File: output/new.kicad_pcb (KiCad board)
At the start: 2 copper layers, 96 parts

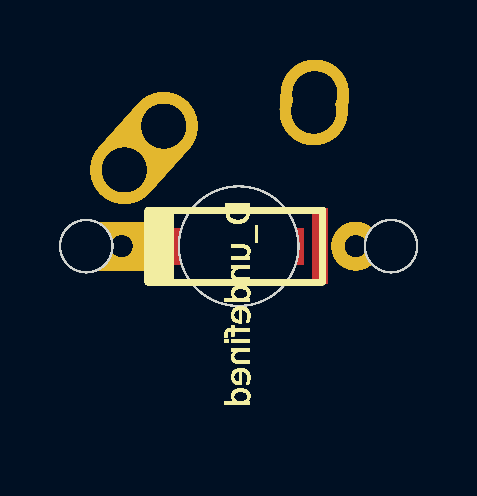
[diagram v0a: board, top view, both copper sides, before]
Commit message: feat: generate PCB component names
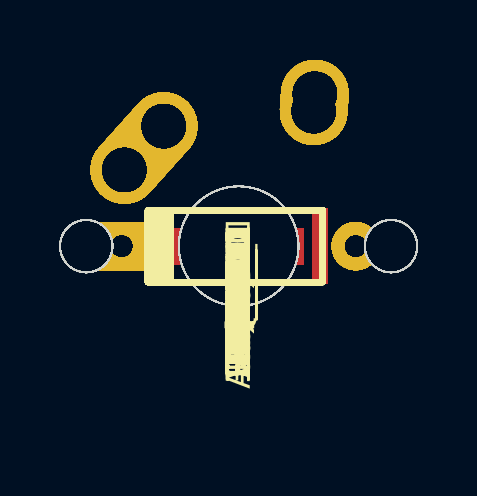
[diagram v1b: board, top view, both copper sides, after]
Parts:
- removed D_undefined (x48): D, keyboard_parts:D_SOD123_axial
- removed K_ (x48): KEYSW, MX_Alps_Hybrid:MX-[object
- added D_A, D_ALT, D_ALT1, D_B, D_BS, D_C, D_CAPS, D_COMMA, D_D, D_DOT, D_E, D_ENTER, D_ESC, D_F, D_FN, D_G, D_H, D_I, D_J, D_K, D_L, D_M, D_M2, D_M3, D_M4, D_N, D_O, D_OPT, D_OPT1, D_P, D_Q, D_QUOTE, D_R, D_S, D_SEMIC, D_SHIFT, D_SHIFT1, D_SLASH, D_SPACE, D_T, D_U, D_V, D_W, D_X, D_Y, D_Z, D_[, D_]: D, keyboard_parts:D_SOD123_axial, F.Cu at (nan, nan)
- added K_A, K_ALT, K_ALT1, K_B, K_BS, K_C, K_CAPS, K_COMMA, K_D, K_DOT, K_E, K_ENTER, K_ESC, K_F, K_FN, K_G, K_H, K_I, K_J, K_K, K_L, K_M, K_M2, K_M3, K_M4, K_N, K_O, K_OPT, K_OPT1, K_P, K_Q, K_QUOTE, K_R, K_S, K_SEMIC, K_SHIFT, K_SHIFT1, K_SLASH, K_SPACE, K_T, K_U, K_V, K_W, K_X, K_Y, K_Z, K_[, K_]: KEYSW, MX_Alps_Hybrid:MX-[object, F.Cu at (nan, nan)

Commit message: feat: PCB keyboard layout
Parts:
- removed D_[, D_]: D, keyboard_parts:D_SOD123_axial
- removed the K_A at (nan, nan)
- removed the K_ALT at (nan, nan)
- removed the K_B at (nan, nan)
- removed the K_BS at (nan, nan)
- removed the K_C at (nan, nan)
- removed the K_CAPS at (nan, nan)
- removed the K_COMMA at (nan, nan)
- removed the K_D at (nan, nan)
- removed the K_DOT at (nan, nan)
- removed the K_E at (nan, nan)
- removed the K_ENTER at (nan, nan)
- removed the K_ESC at (nan, nan)
- removed the K_F at (nan, nan)
- removed the K_FN at (nan, nan)
- removed the K_G at (nan, nan)
- removed the K_H at (nan, nan)
- removed the K_I at (nan, nan)
- removed the K_J at (nan, nan)
- removed the K_K at (nan, nan)
- removed the K_L at (nan, nan)
- removed the K_M at (nan, nan)
- removed the K_N at (nan, nan)
- removed the K_O at (nan, nan)
- removed the K_OPT at (nan, nan)
- removed the K_P at (nan, nan)
- removed the K_Q at (nan, nan)
- removed the K_QUOTE at (nan, nan)
- removed the K_R at (nan, nan)
- removed the K_S at (nan, nan)
- removed the K_SEMIC at (nan, nan)
- removed the K_SHIFT at (nan, nan)
- removed the K_SLASH at (nan, nan)
- removed the K_SPACE at (nan, nan)
- removed the K_T at (nan, nan)
- removed the K_U at (nan, nan)
- removed the K_V at (nan, nan)
- removed the K_W at (nan, nan)
- removed the K_X at (nan, nan)
- removed the K_Y at (nan, nan)
- removed the K_Z at (nan, nan)
- removed K_[, K_]: KEYSW, MX_Alps_Hybrid:MX-[object
- added D_CBRAC: D, keyboard_parts:D_SOD123_axial, F.Cu at (233.9, 10.0)
- added D_OBRAC: D, keyboard_parts:D_SOD123_axial, F.Cu at (252.9, 10.0)
- added K_A: KEYSW, MX_Alps_Hybrid:MX-1U-NoLED, F.Cu at (57.1, 28.6)
- added K_ALT: KEYSW, MX_Alps_Hybrid:MX-1.25U-NoLED, F.Cu at (83.3, 66.7)
- added K_B: KEYSW, MX_Alps_Hybrid:MX-1U-NoLED, F.Cu at (142.9, 47.6)
- added K_BS: KEYSW, MX_Alps_Hybrid:MX-1U-NoLED, F.Cu at (281.0, 9.53)
- added K_C: KEYSW, MX_Alps_Hybrid:MX-1U-NoLED, F.Cu at (104.8, 47.6)
- added K_CAPS: KEYSW, MX_Alps_Hybrid:MX-1.25U-NoLED, F.Cu at (35.7, 28.6)
- added K_CBRAC: KEYSW, MX_Alps_Hybrid:MX-1U-NoLED, F.Cu at (242.9, 9.53)
- added K_COMMA: KEYSW, MX_Alps_Hybrid:MX-1U-NoLED, F.Cu at (200.0, 47.6)
- added K_D: KEYSW, MX_Alps_Hybrid:MX-1U-NoLED, F.Cu at (95.2, 28.6)
- added K_DOT: KEYSW, MX_Alps_Hybrid:MX-1U-NoLED, F.Cu at (219.1, 47.6)
- added K_E: KEYSW, MX_Alps_Hybrid:MX-1U-NoLED, F.Cu at (90.5, 9.53)
- added K_ENTER: KEYSW, MX_Alps_Hybrid:MX-1.75U-NoLED, F.Cu at (273.8, 28.6)
- added K_ESC: KEYSW, MX_Alps_Hybrid:MX-1U-NoLED, F.Cu at (33.3, 9.53)
- added K_F: KEYSW, MX_Alps_Hybrid:MX-1U-NoLED, F.Cu at (114.3, 28.6)
- added K_FN: KEYSW, MX_Alps_Hybrid:MX-1U-NoLED, F.Cu at (281.0, 47.6)
- added K_G: KEYSW, MX_Alps_Hybrid:MX-1U-NoLED, F.Cu at (133.3, 28.6)
- added K_H: KEYSW, MX_Alps_Hybrid:MX-1U-NoLED, F.Cu at (152.4, 28.6)
- added K_I: KEYSW, MX_Alps_Hybrid:MX-1U-NoLED, F.Cu at (185.7, 9.53)
- added K_J: KEYSW, MX_Alps_Hybrid:MX-1U-NoLED, F.Cu at (171.4, 28.6)
- added K_K: KEYSW, MX_Alps_Hybrid:MX-1U-NoLED, F.Cu at (190.5, 28.6)
- added K_L: KEYSW, MX_Alps_Hybrid:MX-1U-NoLED, F.Cu at (209.6, 28.6)
- added K_M: KEYSW, MX_Alps_Hybrid:MX-1U-NoLED, F.Cu at (181.0, 47.6)
- added K_N: KEYSW, MX_Alps_Hybrid:MX-1U-NoLED, F.Cu at (161.9, 47.6)
- added K_O: KEYSW, MX_Alps_Hybrid:MX-1U-NoLED, F.Cu at (204.8, 9.53)
- added K_OBRAC: KEYSW, MX_Alps_Hybrid:MX-1U-NoLED, F.Cu at (261.9, 9.53)
- added K_OPT: KEYSW, MX_Alps_Hybrid:MX-1U-NoLED, F.Cu at (61.9, 66.7)
- added K_P: KEYSW, MX_Alps_Hybrid:MX-1U-NoLED, F.Cu at (223.8, 9.53)
- added K_Q: KEYSW, MX_Alps_Hybrid:MX-1U-NoLED, F.Cu at (52.4, 9.53)
- added K_QUOTE: KEYSW, MX_Alps_Hybrid:MX-1U-NoLED, F.Cu at (247.7, 28.6)
- added K_R: KEYSW, MX_Alps_Hybrid:MX-1U-NoLED, F.Cu at (109.5, 9.53)
- added K_S: KEYSW, MX_Alps_Hybrid:MX-1U-NoLED, F.Cu at (76.2, 28.6)
- added K_SEMIC: KEYSW, MX_Alps_Hybrid:MX-1U-NoLED, F.Cu at (228.6, 28.6)
- added K_SHIFT: KEYSW, MX_Alps_Hybrid:MX-1.75U-NoLED, F.Cu at (40.5, 47.6)
- added K_SLASH: KEYSW, MX_Alps_Hybrid:MX-1U-NoLED, F.Cu at (238.1, 47.6)
- added K_SPACE: KEYSW, MX_Alps_Hybrid:MX-6.25U-NoLED, F.Cu at (154.8, 66.7)
- added K_T: KEYSW, MX_Alps_Hybrid:MX-1U-NoLED, F.Cu at (128.6, 9.53)
- added K_U: KEYSW, MX_Alps_Hybrid:MX-1U-NoLED, F.Cu at (166.7, 9.53)
- added K_V: KEYSW, MX_Alps_Hybrid:MX-1U-NoLED, F.Cu at (123.8, 47.6)
- added K_W: KEYSW, MX_Alps_Hybrid:MX-1U-NoLED, F.Cu at (71.4, 9.53)
- added K_X: KEYSW, MX_Alps_Hybrid:MX-1U-NoLED, F.Cu at (85.7, 47.6)
- added K_Y: KEYSW, MX_Alps_Hybrid:MX-1U-NoLED, F.Cu at (147.6, 9.53)
- added K_Z: KEYSW, MX_Alps_Hybrid:MX-1U-NoLED, F.Cu at (66.7, 47.6)
- K_ALT1, K_SHIFT1: footprint MX_Alps_Hybrid:MX-[object -> MX_Alps_Hybrid:MX-1.25U-NoLED
- K_M2, K_M3, K_M4, K_OPT1: footprint MX_Alps_Hybrid:MX-[object -> MX_Alps_Hybrid:MX-1U-NoLED

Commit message: feat: added planes and frames to the PCB
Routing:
- added copper zone on F.Cu, net GND
- added copper zone on B.Cu, net VCC
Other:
- board outline added: 298.5 x 84.2 mm
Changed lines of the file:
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@@
       (net 311 "Net-(D_OPT1-Pad2)"))
   )
+  (gr_line (start -4 -4) (end 294.5125 -4) (layer Edge.Cuts) (width 0.2))
+  (gr_line (start 294.5125 -4) (end 294.5125 80.2) (layer Edge.Cuts) (width 0.2))
+  (gr_line (start 294.5125 80.2) (end -4 80.2) (layer Edge.Cuts) (width 0.2))
+  (gr_line (start -4 80.2) (end -4 -4) (layer Edge.Cuts) (width 0.2))
+  (gr_arc (start -4 -4) (end -4 -4) (angle -90) (layer Edge.Cuts) (width 0.2))
+  (gr_arc (start 294.5125 -4) (end 294.5125 -4) (angle 90) (layer Edge.Cuts) (width 0.2))
+  (gr_arc (start 294.5125 80.2) (end 294.5125 80.2) (angle -90) (layer Edge.Cuts) (width 0.2))
+  (gr_arc (start -4 80.2) (end -4 80.2) (angle 90) (layer Edge.Cuts) (width 0.2))
+  (zone (net 0) (net_name GND) (layer F.Cu) (hatch edge 0.508)
+    (connect_pads (clearance 0.508))
+    (min_thickness 0.254)
+    (fill yes (arc_segments 16) (thermal_gap 0.508) (thermal_bridge_width 0.508))
+    (polygon
+      (pts
+        (xy -5 -5) (xy -5 81.2) (xy 295.5125 81.2) (xy 295.5125 -5)
+      )
+    )
+  )
+  (zone (net 0) (net_name VCC) (layer B.Cu) (hatch edge 0.508)
+    (connect_pads (clearance 0.508))
+    (min_thickness 0.254)
+    (fill yes (arc_segments 16) (thermal_gap 0.508) (thermal_bridge_width 0.508))
+    (polygon
+      (pts
+        (xy -5 -5) (xy -5 81.2) (xy 295.5125 81.2) (xy 295.5125 -5)
+      )
+    )
+  )
 )

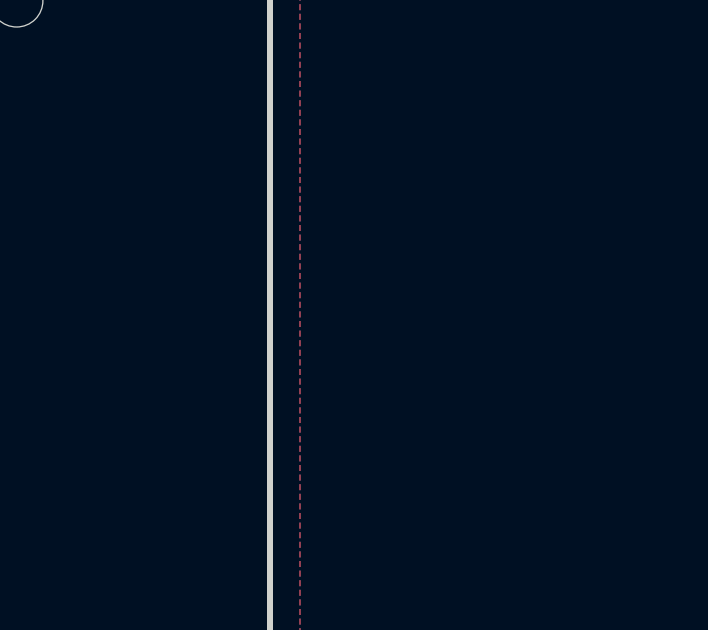
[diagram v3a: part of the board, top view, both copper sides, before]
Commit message: feat: crystal and crystal caps
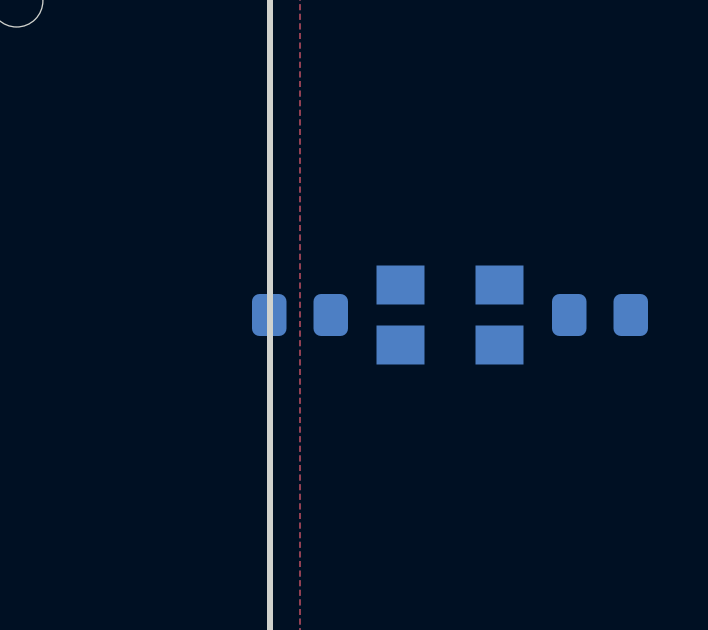
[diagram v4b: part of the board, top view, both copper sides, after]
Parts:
- added C100: 22pF, Capacitor_SMD:C_0805_2012Metric_Pad1.15x1.40mm_HandSolder, B.Cu at (295.5, 20.0)
- added C101: 22pF, Capacitor_SMD:C_0805_2012Metric_Pad1.15x1.40mm_HandSolder, B.Cu at (305.5, 20.0)
- added X102: XTAL_GND, Crystal:Crystal_SMD_5032-4Pin_5.0x3.2mm, B.Cu at (300.5, 20.0)
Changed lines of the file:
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@@
   (net 310 "Net-(D_OPT1-Pad1)")
   (net 311 "Net-(D_OPT1-Pad2)")
+  (net 312 "Net-(C100-Pad1)")
+  (net 313 "Net-(C100-Pad2)")
+  (net 314 "Net-(C101-Pad1)")
+  (net 315 "Net-(C101-Pad2)")
+  (net 316 "Net-(X102-Pad1)")
+  (net 317 "Net-(X102-Pad2)")
+  (net 318 "Net-(X102-Pad3)")
+  (net 319 "Net-(X102-Pad4)")
 (net_class Default "This is the default net class."
   (clearance 0.2)
@@
   (add_net "Net-(D_OPT1-Pad1)")
   (add_net "Net-(D_OPT1-Pad2)")
+  (add_net "Net-(C100-Pad1)")
+  (add_net "Net-(C100-Pad2)")
+  (add_net "Net-(C101-Pad1)")
+  (add_net "Net-(C101-Pad2)")
+  (add_net "Net-(X102-Pad1)")
+  (add_net "Net-(X102-Pad2)")
+  (add_net "Net-(X102-Pad3)")
+  (add_net "Net-(X102-Pad4)")
 )
   (module MX_Alps_Hybrid:MX-1U-NoLED (layer F.Cu)
@@
     )
   )
+  (module Capacitor_SMD:C_0805_2012Metric_Pad1.15x1.40mm_HandSolder (layer B.Cu)
+    (at 295.5125 20 )
+    (descr "Capacitor SMD 0805 (2012 Metric), square (rectangular) end terminal, IPC_7351 nominal with elongated pad for handsoldering. (Body size source: https://docs.google.com/spreadsheets/d/1BsfQQcO9C6DZCsRaXUlFlo91Tg2WpOkGARC1WS5S8t0/edit?usp=sharing), generated with kicad-footprint-generator")
+    (tags "capacitor handsolder")
+    (attr smd)
+    (fp_text reference C100 (at 0 1.65 ) (layer B.SilkS)
+      (effects (font (size 1 1) (thickness 0.15)) (justify mirror))
+    )
+    (fp_text value 22pF (at 0 -1.65 ) (layer B.Fab)
+      (effects (font (size 1 1) (thickness 0.15)) (justify mirror))
+    )
+    (fp_text user %R (at 0 0 ) (layer B.Fab)
+      (effects (font (size 0.5 0.5) (thickness 0.08)) (justify mirror))
+    )
+    (fp_line (start 1.85 -0.95) (end -1.85 -0.95) (layer B.CrtYd) (width 0.05))
+    (fp_line (start 1.85 0.95) (end 1.85 -0.95) (layer B.CrtYd) (width 0.05))
+    (fp_line (start -1.85 0.95) (end 1.85 0.95) (layer B.CrtYd) (width 0.05))
+    (fp_line (start -1.85 -0.95) (end -1.85 0.95) (layer B.CrtYd) (width 0.05))
+    (fp_line (start -0.261252 -0.71) (end 0.261252 -0.71) (layer B.SilkS) (width 0.12))
+    (fp_line (start -0.261252 0.71) (end 0.261252 0.71) (layer B.SilkS) (width 0.12))
+    (fp_line (start 1 -0.6) (end -1 -0.6) (layer B.Fab) (width 0.1))
+    (fp_line (start 1 0.6) (end 1 -0.6) (layer B.Fab) (width 0.1))
+    (fp_line (start -1 0.6) (end 1 0.6) (layer B.Fab) (width 0.1))
+    (fp_line (start -1 -0.6) (end -1 0.6) (layer B.Fab) (width 0.1))
+    (pad 1 smd roundrect (at -1.025 0 ) (size 1.15 1.4) (layers B.Cu B.Paste B.Mask) (roundrect_rratio 0.217391)
+      (net 312 "Net-(C100-Pad1)"))
+    (pad 2 smd roundrect (at 1.025 0 ) (size 1.15 1.4) (layers B.Cu B.Paste B.Mask) (roundrect_rratio 0.217391)
+      (net 1 GND))
+    (model ${KISYS3DMOD}/Capacitor_SMD.3dshapes/C_0805_2012Metric.wrl
+      (at (xyz 0 0 0))
+      (scale (xyz 1 1 1))
+      (rotate (xyz 0 0 0))
+    )
+  )
+  (module Capacitor_SMD:C_0805_2012Metric_Pad1.15x1.40mm_HandSolder (layer B.Cu)
+    (at 305.5125 20 )
+    (descr "Capacitor SMD 0805 (2012 Metric), square (rectangular) end terminal, IPC_7351 nominal with elongated pad for handsoldering. (Body size source: https://docs.google.com/spreadsheets/d/1BsfQQcO9C6DZCsRaXUlFlo91Tg2WpOkGARC1WS5S8t0/edit?usp=sharing), generated with kicad-footprint-generator")
+    (tags "capacitor handsolder")
+    (attr smd)
+    (fp_text reference C101 (at 0 1.65 ) (layer B.SilkS)
+      (effects (font (size 1 1) (thickness 0.15)) (justify mirror))
+    )
+    (fp_text value 22pF (at 0 -1.65 ) (layer B.Fab)
+      (effects (font (size 1 1) (thickness 0.15)) (justify mirror))
+    )
+    (fp_text user %R (at 0 0 ) (layer B.Fab)
+      (effects (font (size 0.5 0.5) (thickness 0.08)) (justify mirror))
+    )
+    (fp_line (start 1.85 -0.95) (end -1.85 -0.95) (layer B.CrtYd) (width 0.05))
+    (fp_line (start 1.85 0.95) (end 1.85 -0.95) (layer B.CrtYd) (width 0.05))
+    (fp_line (start -1.85 0.95) (end 1.85 0.95) (layer B.CrtYd) (width 0.05))
+    (fp_line (start -1.85 -0.95) (end -1.85 0.95) (layer B.CrtYd) (width 0.05))
+    (fp_line (start -0.261252 -0.71) (end 0.261252 -0.71) (layer B.SilkS) (width 0.12))
+    (fp_line (start -0.261252 0.71) (end 0.261252 0.71) (layer B.SilkS) (width 0.12))
+    (fp_line (start 1 -0.6) (end -1 -0.6) (layer B.Fab) (width 0.1))
+    (fp_line (start 1 0.6) (end 1 -0.6) (layer B.Fab) (width 0.1))
+    (fp_line (start -1 0.6) (end 1 0.6) (layer B.Fab) (width 0.1))
+    (fp_line (start -1 -0.6) (end -1 0.6) (layer B.Fab) (width 0.1))
+    (pad 1 smd roundrect (at -1.025 0 ) (size 1.15 1.4) (layers B.Cu B.Paste B.Mask) (roundrect_rratio 0.217391)
+      (net 314 "Net-(C101-Pad1)"))
+    (pad 2 smd roundrect (at 1.025 0 ) (size 1.15 1.4) (layers B.Cu B.Paste B.Mask) (roundrect_rratio 0.217391)
+      (net 1 GND))
+    (model ${KISYS3DMOD}/Capacitor_SMD.3dshapes/C_0805_2012Metric.wrl
+      (at (xyz 0 0 0))
+      (scale (xyz 1 1 1))
+      (rotate (xyz 0 0 0))
+    )
+  )
+(module Crystal:Crystal_SMD_5032-4Pin_5.0x3.2mm (layer B.Cu)
+    (at 300.5125 20 )
+    (descr "SMD Crystal SERIES SMD2520/4 http://www.icbase.com/File/PDF/HKC/HKC00061008.pdf, 5.0x3.2mm^2 package")
+    (tags "SMD SMT crystal")
+    (attr smd)
+    (fp_text reference X102 (at 0 2.8 ) (layer B.SilkS)
+      (effects (font (size 1 1) (thickness 0.15)) (justify mirror))
+    )
+    (fp_text value XTAL_GND (at 0 -2.8 ) (layer B.Fab)
+      (effects (font (size 1 1) (thickness 0.15)) (justify mirror))
+    )
+    (fp_text user %R (at 0 0 ) (layer B.Fab)
+      (effects (font (size 1 1) (thickness 0.15)) (justify mirror))
+    )
+    (fp_line (start -2.3 1.6) (end 2.3 1.6) (layer B.Fab) (width 0.1))
+    (fp_line (start 2.3 1.6) (end 2.5 1.4) (layer B.Fab) (width 0.1))
+    (fp_line (start 2.5 1.4) (end 2.5 -1.4) (layer B.Fab) (width 0.1))
+    (fp_line (start 2.5 -1.4) (end 2.3 -1.6) (layer B.Fab) (width 0.1))
+    (fp_line (start 2.3 -1.6) (end -2.3 -1.6) (layer B.Fab) (width 0.1))
+    (fp_line (start -2.3 -1.6) (end -2.5 -1.4) (layer B.Fab) (width 0.1))
+    (fp_line (start -2.5 -1.4) (end -2.5 1.4) (layer B.Fab) (width 0.1))
+    (fp_line (start -2.5 1.4) (end -2.3 1.6) (layer B.Fab) (width 0.1))
+    (fp_line (start -2.5 -0.6) (end -1.5 -1.6) (layer B.Fab) (width 0.1))
+    (fp_line (start -2.65 1.85) (end -2.65 -1.85) (layer B.SilkS) (width 0.12))
+    (fp_line (start -2.65 -1.85) (end 2.65 -1.85) (layer B.SilkS) (width 0.12))
+    (fp_line (start -2.8 1.9) (end -2.8 -1.9) (layer B.CrtYd) (width 0.05))
+    (fp_line (start -2.8 -1.9) (end 2.8 -1.9) (layer B.CrtYd) (width 0.05))
+    (fp_line (start 2.8 -1.9) (end 2.8 1.9) (layer B.CrtYd) (width 0.05))
+    (fp_line (start 2.8 1.9) (end -2.8 1.9) (layer B.CrtYd) (width 0.05))
+    (pad 1 smd rect (at -1.65 -1 ) (size 1.6 1.3) (layers B.Cu B.Paste B.Mask)
+      (net 315 "Net-(C101-Pad2)"))
+    (pad 2 smd rect (at 1.65 -1 ) (size 1.6 1.3) (layers B.Cu B.Paste B.Mask)
+      (net 317 "Net-(X102-Pad2)"))
+    (pad 3 smd rect (at 1.65 1 ) (size 1.6 1.3) (layers B.Cu B.Paste B.Mask)
+      (net 1 GND))
+    (pad 4 smd rect (at -1.65 1 ) (size 1.6 1.3) (layers B.Cu B.Paste B.Mask)
+      (net 319 "Net-(X102-Pad4)"))
+    (model ${KISYS3DMOD}/Crystal.3dshapes/Crystal_SMD_5032-4Pin_5.0x3.2mm.wrl
+      (at (xyz 0 0 0))
+      (scale (xyz 1 1 1))
+      (rotate (xyz 0 0 0))
+    )
+  )

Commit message: feat: all components added to PCB
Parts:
- removed C100, C101: 22pF, Capacitor_SMD:C_0805_2012Metric_Pad1.15x1.40mm_HandSolder
- removed X102: XTAL_GND, Crystal:Crystal_SMD_5032-4Pin_5.0x3.2mm
- added C1: 22pF, Capacitor_SMD:C_0805_2012Metric_Pad1.15x1.40mm_HandSolder, B.Cu at (295.5, 20.0)
- added C2: 22pF, Capacitor_SMD:C_0805_2012Metric_Pad1.15x1.40mm_HandSolder, B.Cu at (305.5, 20.0)
- added C3: 22pF, Capacitor_SMD:C_0805_2012Metric_Pad1.15x1.40mm_HandSolder, B.Cu at (295.5, 5.00)
- added C4: 22pF, Capacitor_SMD:C_0805_2012Metric_Pad1.15x1.40mm_HandSolder, B.Cu at (295.5, 30.0)
- added C5: 22pF, Capacitor_SMD:C_0805_2012Metric_Pad1.15x1.40mm_HandSolder, B.Cu at (300.5, 30.0)
- added C6: 22pF, Capacitor_SMD:C_0805_2012Metric_Pad1.15x1.40mm_HandSolder, B.Cu at (305.5, 30.0)
- added C7: 22pF, Capacitor_SMD:C_0805_2012Metric_Pad1.15x1.40mm_HandSolder, B.Cu at (310.5, 30.0)
- added R1: 10k, Resistor_SMD:R_0805_2012Metric_Pad1.15x1.40mm_HandSolder, B.Cu at (304.5, -5.00)
- added R2: 10k, Resistor_SMD:R_0805_2012Metric_Pad1.15x1.40mm_HandSolder, B.Cu at (315.5, 8.00)
- added R3: 22u, Resistor_SMD:R_0805_2012Metric_Pad1.15x1.40mm_HandSolder, B.Cu at (295.5, 8.00)
- added R4: 22u, Resistor_SMD:R_0805_2012Metric_Pad1.15x1.40mm_HandSolder, B.Cu at (295.5, 12.0)
- added SW1: SW_PUSH, Button_Switch_SMD:SW_SPST_TL3342, B.Cu at (304.5, -10.0)
- added U1: ATMEGA32U4, Package_QFP:TQFP-44_10x10mm_P0.8mm, B.Cu at (304.5, 5.00)
- added USB1: USB_mini_micro_B, keyboard_parts:USB_miniB_hirose_5S8, B.Cu at (145.3, 2.00)
- added X1: XTAL_GND, Crystal:Crystal_SMD_5032-4Pin_5.0x3.2mm, B.Cu at (300.5, 20.0)
